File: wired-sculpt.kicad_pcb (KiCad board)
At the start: 2 copper layers, 40 x 50 mm, 39 parts, among them J1 10103594-0001LF, J2 FFC3B07-30-T, J3 AVR-ISP-6 - NOT FITTED, Q1 BSS84AK,215, Q2 2N7002BK, SW1 FSMSM, SW2 S2B-PH-K-S(LF)(SN), U1 USBLC6-2SC6, U2 LM2776DBVT, U3 AT90USB1286-AU, Y1 TSX-3225 16.0000MF18X-AC0

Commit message: Fix linkage of AT90 symbol
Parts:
- C7, C8: value 06035A160JAT2A -> CL10C160JB8NNNC
- R11: value ERJ-PA3J560V -> ERJ-PA3J151V
- R12: value ERJ-PA3F22R0V -> ERJ-PA3J151V
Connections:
- J1 pad 4: Net-(J1-Pad4) -> unconnected-(J1-Pad4)
- U3 pad 1: Net-(U3-Pad1) -> unconnected-(U3-Pad1)
- U3 pad 14: Net-(U3-Pad14) -> unconnected-(U3-Pad14)
- U3 pad 18: Net-(U3-Pad18) -> unconnected-(U3-Pad18)
- U3 pad 19: Net-(U3-Pad19) -> unconnected-(U3-Pad19)
- U3 pad 2: Net-(U3-Pad2) -> unconnected-(U3-Pad2)
- U3 pad 25: Net-(U3-Pad25) -> unconnected-(U3-Pad25)
- U3 pad 26: Net-(U3-Pad26) -> unconnected-(U3-Pad26)
- U3 pad 27: Net-(U3-Pad27) -> unconnected-(U3-Pad27)
- U3 pad 58: Net-(U3-Pad58) -> unconnected-(U3-Pad58)
- U3 pad 59: Net-(U3-Pad59) -> unconnected-(U3-Pad59)
- U3 pad 60: Net-(U3-Pad60) -> unconnected-(U3-Pad60)
- U3 pad 61: Net-(U3-Pad61) -> unconnected-(U3-Pad61)
- U3 pad 62: Net-(U3-Pad62) -> unconnected-(U3-Pad62)
- U3 pad 9: Net-(U3-Pad9) -> unconnected-(U3-Pad9)

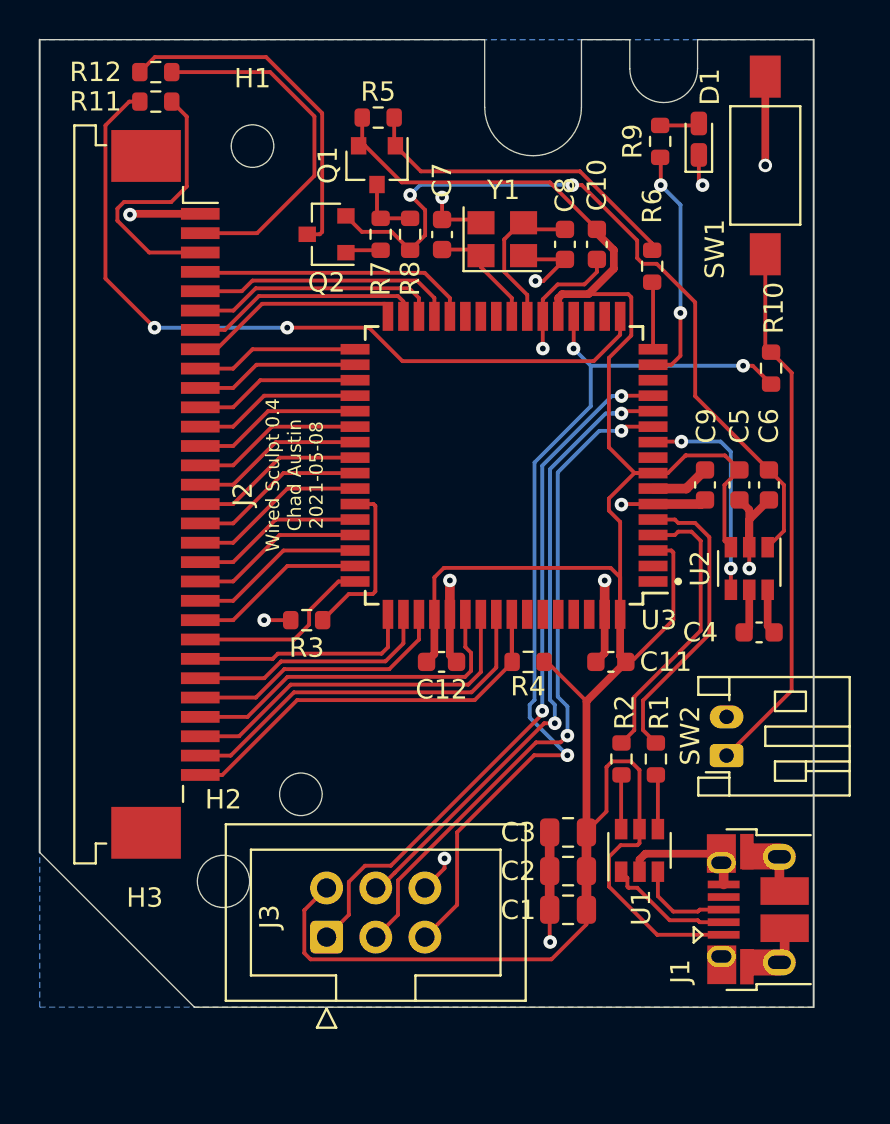
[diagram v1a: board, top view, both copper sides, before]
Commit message: Extend PCB to fully match original
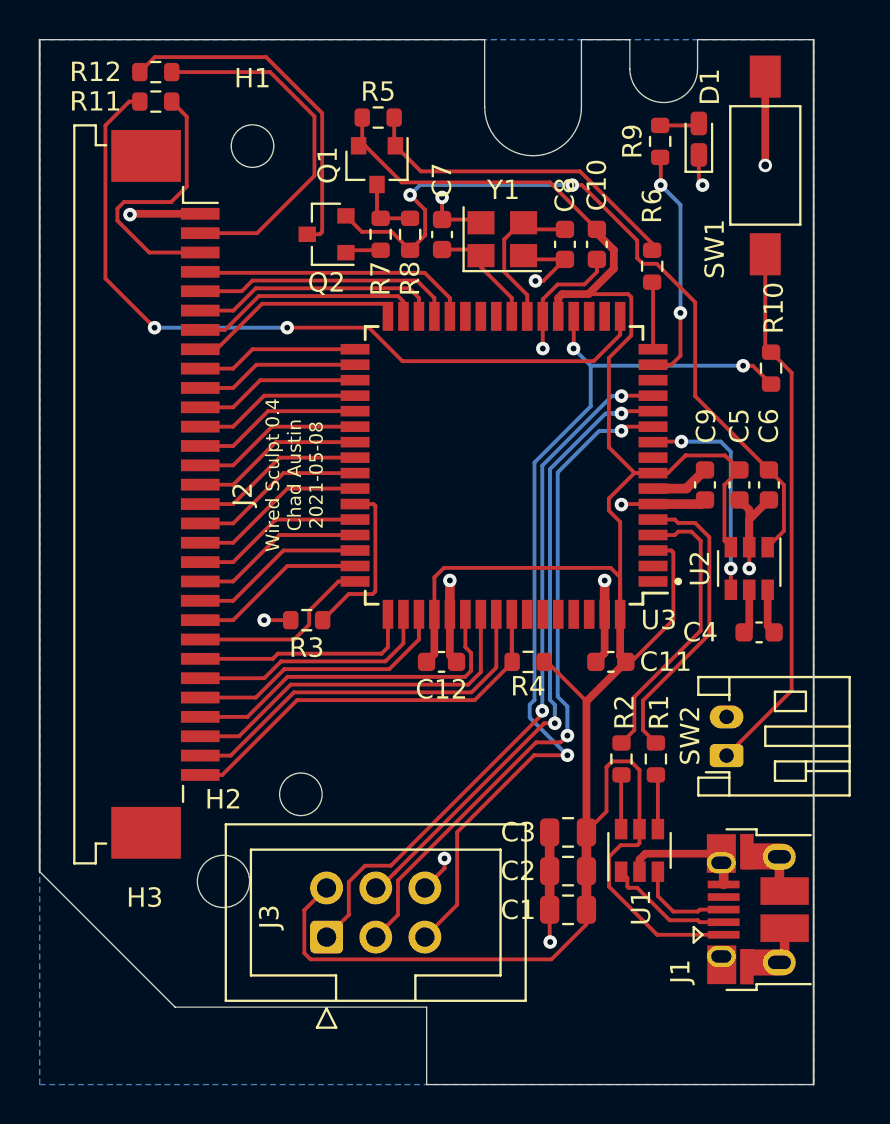
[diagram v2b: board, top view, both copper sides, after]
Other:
- board size 40 x 50 mm -> 40 x 54 mm
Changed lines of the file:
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@@
   (gr_line (start 154 30) (end 154 31.5) (layer "Edge.Cuts") (width 0.05))
   (gr_line (start 150.5 31.5) (end 150.5 30) (layer "Edge.Cuts") (width 0.05))
-  (gr_line (start 128 80) (end 120 72) (layer "Edge.Cuts") (width 0.05))
+  (gr_line (start 127 80) (end 120 73) (layer "Edge.Cuts") (width 0.05))
   (gr_line (start 143 30) (end 143 33.5) (layer "Edge.Cuts") (width 0.05))
   (gr_arc (start 154 31.5) (mid 152.25 33.25) (end 150.5 31.5) (layer "Edge.Cuts") (width 0.05))
   (gr_line (start 160 30) (end 154 30) (layer "Edge.Cuts") (width 0.05))
-  (gr_line (start 120 72) (end 120 30) (layer "Edge.Cuts") (width 0.1))
-  (gr_line (start 160 30) (end 160 80) (layer "Edge.Cuts") (width 0.1))
+  (gr_line (start 120 73) (end 120 30) (layer "Edge.Cuts") (width 0.1))
+  (gr_line (start 160 30) (end 160 84) (layer "Edge.Cuts") (width 0.1))
   (gr_line (start 148 30) (end 150.5 30) (layer "Edge.Cuts") (width 0.05))
   (gr_arc (start 148 33.5) (mid 145.5 36) (end 143 33.5) (layer "Edge.Cuts") (width 0.05))
-  (gr_line (start 160 80) (end 128 80) (layer "Edge.Cuts") (width 0.05))
+  (gr_line (start 140 84) (end 140 80) (layer "Edge.Cuts") (width 0.05))
+  (gr_line (start 160 84) (end 140 84) (layer "Edge.Cuts") (width 0.05))
+  (gr_line (start 140 80) (end 127 80) (layer "Edge.Cuts") (width 0.05))
   (gr_line (start 148 30) (end 148 33.5) (layer "Edge.Cuts") (width 0.05))
   (gr_text "Wired Sculpt 0.4\nChad Austin\n2021-05-08" (at 133.177 52.504 90) (layer "F.SilkS")
@@
   (zone (net 1) (net_name "GND") (layer "B.Cu") (hatch edge 0.508)
     (connect_pads thru_hole_only (clearance 0.2))
-    (min_thickness 0.2)
+    (min_thickness 0.2) (filled_areas_thickness no)
     (fill yes (thermal_gap 0.2) (thermal_bridge_width 0.5))
     (polygon
       (pts
-        (xy 160 80)
-        (xy 120 80)
+        (xy 160 84)
+        (xy 120 84)
         (xy 120 30)
         (xy 160 30)

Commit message: Redo layout to resolve some DRC errors
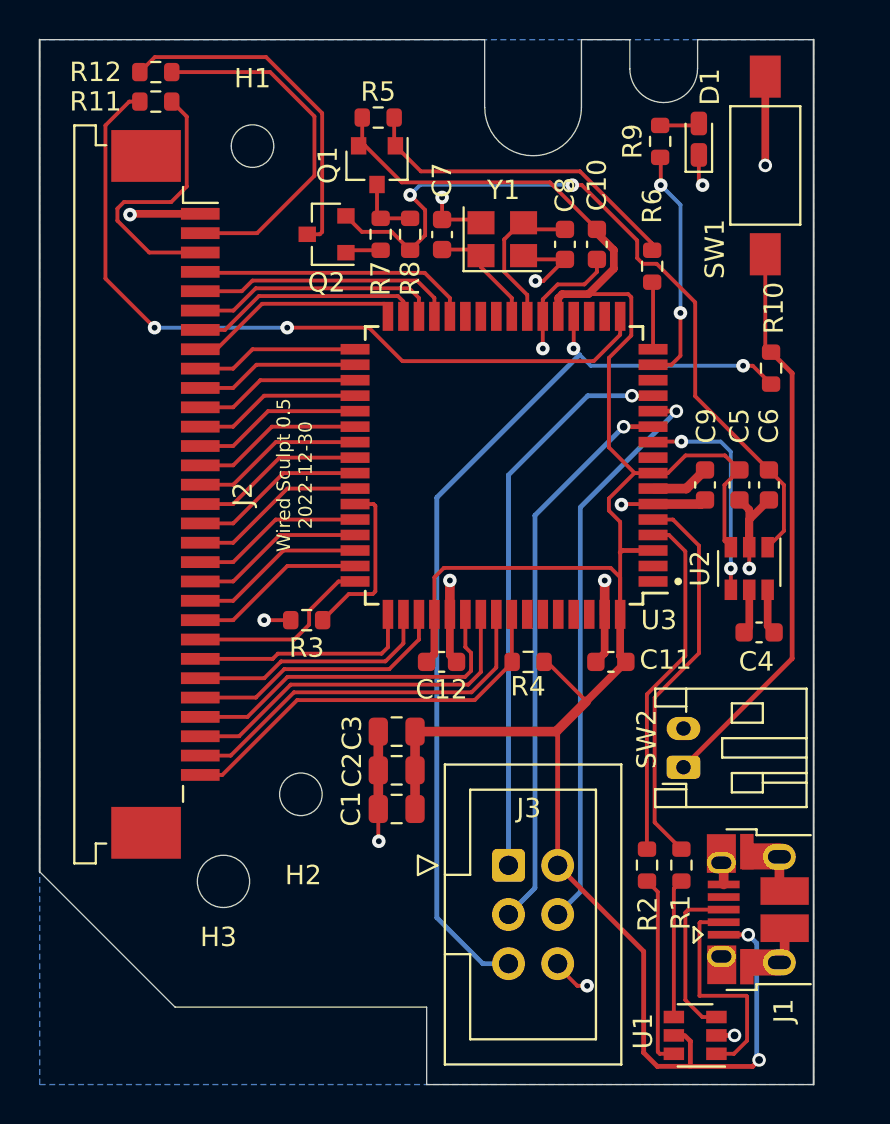
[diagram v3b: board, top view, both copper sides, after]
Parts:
- moved C1 10.3 mm to (138.4, 69.8)
- moved C2 10.3 mm to (138.4, 67.8)
- moved C3 10.3 mm to (138.4, 65.8)
- moved J3 10.1 mm to (144.2, 72.7), turned to 0 degrees
- moved U1 9.98 mm to (153.9, 81.5), turned to 180 degrees
- moved R1 5.64 mm to (153.2, 72.7)
- moved R2 5.64 mm to (151.4, 72.7)
- moved SW2 2.31 mm to (153.3, 67.6)
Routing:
- net VBUS: track 138.6 -> 127.7 mm, vias 0 -> 2
- net MISO: track 37.0 -> 29.3 mm, vias 2 -> 1
- net /Dout-: track 2.81 -> 9.93 mm
- net SCK: track 35.0 -> 29.2 mm, vias 2 -> 1
- net GND: track 62.8 -> 57.1 mm, vias 13 -> 14
- net /Din-: track 6.64 -> 11.6 mm
- net /D+: track 15.6 -> 20.1 mm
- net /Dout+: track 2.85 -> 7.19 mm
- net /Din+: track 5.03 -> 8.53 mm
- net /D-: track 14.9 -> 18.2 mm
- net MOSI: track 33.1 -> 29.8 mm, vias 2 -> 1
- net PF4: track 24.0 -> 21.0 mm
- net Net-(J2-Pad8): track 11.2 -> 9.68 mm
- net Net-(R10-Pad2): track 27.9 -> 29.4 mm
- net RST: track 48.3 -> 49.5 mm, vias 3 -> 2
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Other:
- rule pad_to_mask_clearance: 0.0508 -> 0
- board text added: "Wired Sculpt 0.5 2022-12-30"
- board text removed: "Wired Sculpt 0.4 Chad Austin 2021-05-08"

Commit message: Add MPN to all components
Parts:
- C1: value CL21A475KOFNNNE -> 4.7uF
- C10, C11, C12: value CL10B104KB8NNNC -> 0.1uF
- C2: value CL21B104KACNNNC -> 0.1uF
- C3: value CL21B103KBANNNC -> 10nF
- C4, C5, C6, C9: value CL10A105KA8NNNC -> 1uF
- C7, C8: value CL10C160JB8NNNC -> 16pF
- D1: value 150080GS75000 -> green led
- J1: value 10103594-0001LF -> USB Micro
- J2: value FFC3B07-30-T -> FFC 30pin
- Q1: value BSS84AK,215 -> P-MOSFET
- Q2: value 2N7002BK -> N-MOSFET
- R1, R2, R7: value ERJ-PA3F22R0V -> 22
- R10, R6, R9: value ERJ-3GEYJ331V -> 330
- R11, R12: value ERJ-PA3J151V -> 150
- R3, R8: value ERJ-PA3J472V -> 4.7k
- R4: value ERJ-3EKF8873V -> 887k
- R5: value ERJ-PA3J473V -> 47k
- SW1: value FSMSM -> Button
- SW2: value S2B-PH-K-S(LF)(SN) -> JST connector
- U1: value USBLC6-2SC6 -> ESD Protection
- Y1: value TSX-3225 16.0000MF18X-AC0 -> Crystal 16MHz
